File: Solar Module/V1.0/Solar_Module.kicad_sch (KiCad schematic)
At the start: 8 parts, among them U1 MT3608

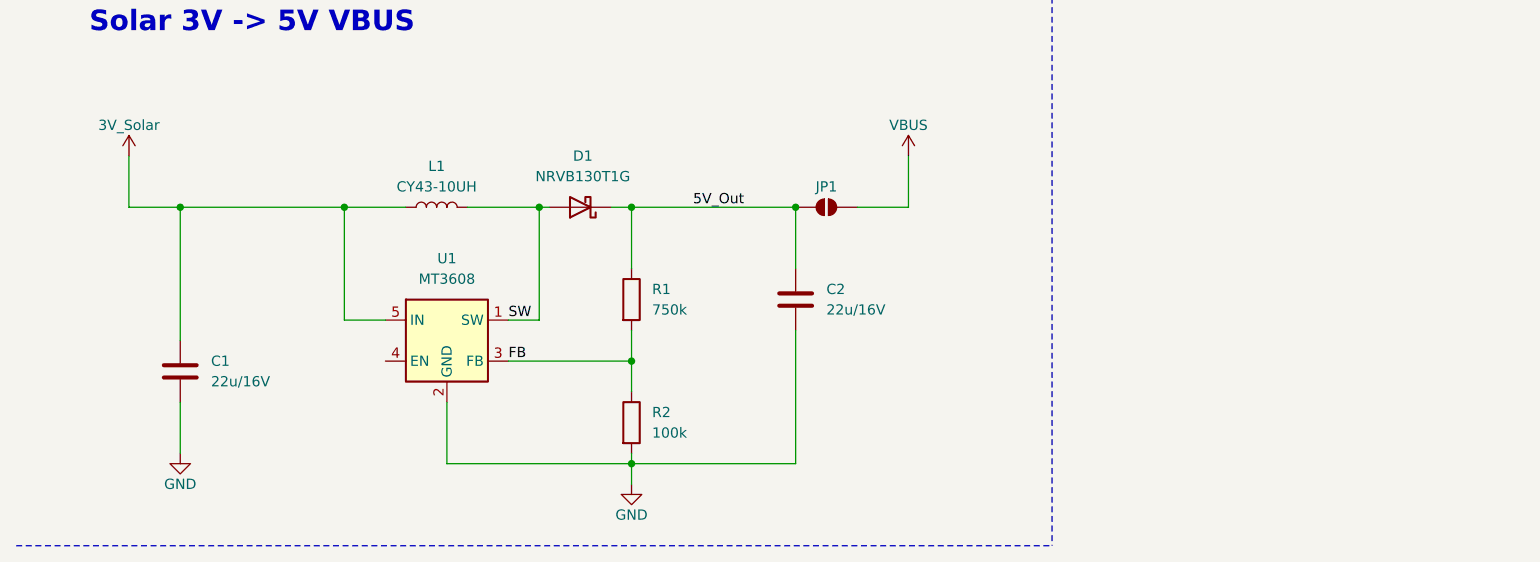
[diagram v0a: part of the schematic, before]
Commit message: Added TP4057 to Schematic.
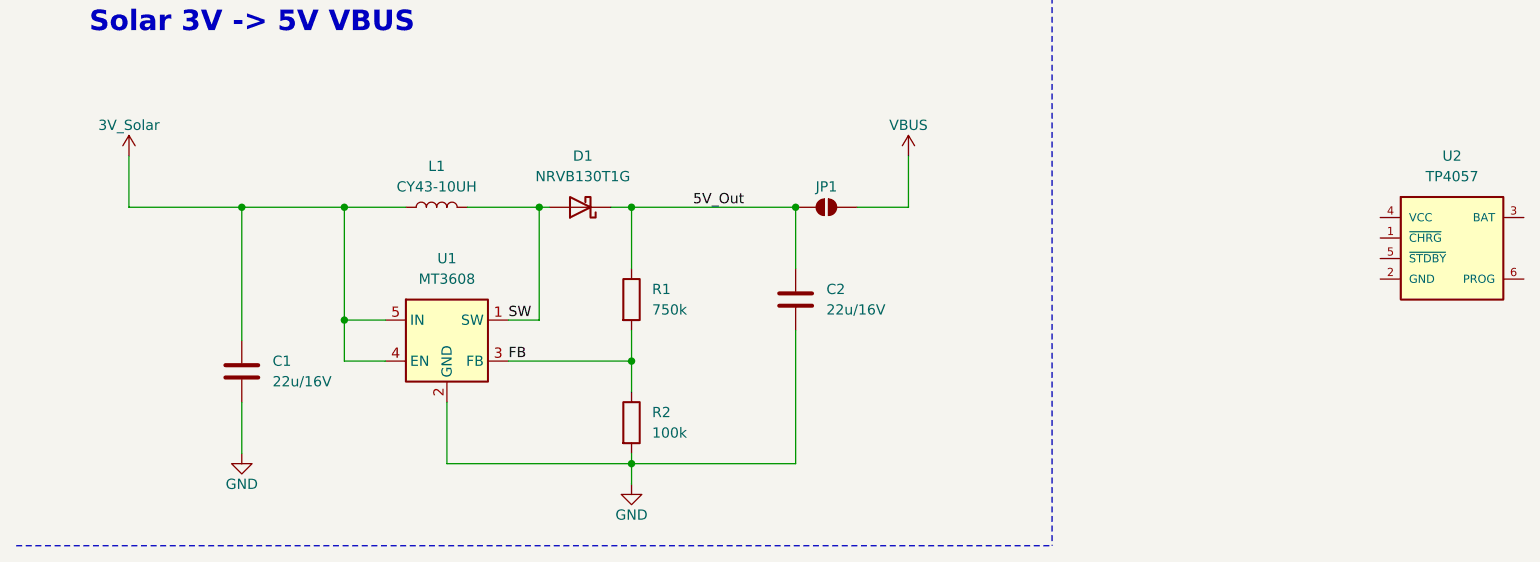
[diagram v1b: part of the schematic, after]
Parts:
- added U2: TP4057, Package_TO_SOT_SMD:SOT-23-6, symbol Private_Power_Modules:TP4057
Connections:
- net 3V_Solar: now also U1.4 (EN)
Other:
- moved on the sheet: C1
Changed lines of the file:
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@@
+	)
+	(junction
+		(at 39.37 46.99)
+		(diameter 0)
+		(color 0 0 0 0)
 	)
 	(junction
@@
 	)
 	(junction
-		(at 31.75 46.99)
-		(diameter 0)
-		(color 0 0 0 0)
-	)
-	(junction
 		(at 52.07 46.99)
 		(diameter 0)
@@
 		(color 0 0 0 0)
 	)
+	(junction
+		(at 52.07 60.96)
+		(diameter 0)
+		(color 0 0 0 0)
+	)
 	(polyline
 		(pts
@@
 	(wire
 		(pts
-			(xy 31.75 46.99) (xy 52.07 46.99)
-		)
-		(stroke
-			(width 0)
-			(type default)
-		)
-	)
-	(wire
-		(pts
 			(xy 52.07 60.96) (xy 57.15 60.96)
 		)
@@
 	(wire
 		(pts
-			(xy 31.75 46.99) (xy 31.75 63.5)
+			(xy 39.37 46.99) (xy 39.37 63.5)
 		)
 		(stroke
@@
 	(wire
 		(pts
-			(xy 31.75 46.99) (xy 25.4 46.99)
+			(xy 25.4 46.99) (xy 39.37 46.99)
 		)
 		(stroke
@@
 	(wire
 		(pts
-			(xy 31.75 71.12) (xy 31.75 77.47)
+			(xy 39.37 71.12) (xy 39.37 77.47)
 		)
 		(stroke
@@
 		(pts
 			(xy 52.07 46.99) (xy 59.69 46.99)
+		)
+		(stroke
+			(width 0)
+			(type default)
+		)
+	)
+	(wire
+		(pts
+			(xy 52.07 66.04) (xy 52.07 60.96)
+		)
+		(stroke
+			(width 0)
+			(type default)
+		)
+	)
+	(wire
+		(pts
+			(xy 57.15 66.04) (xy 52.07 66.04)
+		)
+		(stroke
+			(width 0)
+			(type default)
+		)
+	)
+	(wire
+		(pts
+			(xy 39.37 46.99) (xy 52.07 46.99)
 		)
 		(stroke
@@
 	(symbol
 		(lib_id "power:GND")
-		(at 31.75 77.47 0)
+		(at 39.37 77.47 0)
 		(unit 1)
 		(exclude_from_sim no)
@@
 		(dnp no)
 		(property "Reference" "#PWR02"
-			(at 31.75 83.82 0)
+			(at 39.37 83.82 0)
 			(effects
 				(font
@@
 		)
 		(property "Value" "GND"
-			(at 31.75 81.28 0)
+			(at 39.37 81.28 0)
 			(effects
 				(font
@@
 		)
 		(property "Footprint" ""
-			(at 31.75 77.47 0)
+			(at 39.37 77.47 0)
 			(effects
 				(font
@@
 		)
 		(property "Datasheet" ""
-			(at 31.75 77.47 0)
+			(at 39.37 77.47 0)
 			(effects
 				(font
@@
 		)
 		(property "Description" "Power symbol creates a global label with name \"GND\" , ground"
-			(at 31.75 77.47 0)
+			(at 39.37 77.47 0)
 			(effects
 				(font
@@
 	(symbol
 		(lib_id "Device:C")
-		(at 31.75 67.31 0)
+		(at 39.37 67.31 0)
 		(unit 1)
 		(exclude_from_sim no)
@@
 		(fields_autoplaced yes)
 		(property "Reference" "C1"
-			(at 35.56 66.0399 0)
+			(at 43.18 66.0399 0)
 			(effects
 				(font
@@
 		)
 		(property "Value" "22u/16V"
-			(at 35.56 68.5799 0)
+			(at 43.18 68.5799 0)
 			(effects
 				(font
@@
 		)
 		(property "Footprint" ""
-			(at 32.7152 71.12 0)
+			(at 40.3352 71.12 0)
 			(effects
 				(font
@@
 		)
 		(property "Datasheet" "~"
-			(at 31.75 67.31 0)
+			(at 39.37 67.31 0)
 			(effects
 				(font
@@
 		)
 		(property "Description" "Unpolarized capacitor"
-			(at 31.75 67.31 0)
+			(at 39.37 67.31 0)
 			(effects
 				(font
@@
 					(unit 1)
 				)
+			)
+		)
+	)
+	(symbol
+		(lib_id "Private_Power_Modules:TP4057")
+		(at 187.96 50.8 0)
+		(unit 1)
+		(exclude_from_sim no)
+		(in_bom yes)
+		(on_board yes)
+		(dnp no)
+		(fields_autoplaced yes)
+		(property "Reference" "U2"
+			(at 189.23 40.64 0)
+			(effects
+				(font
+					(size 1.27 1.27)
+				)
+			)
+		)
+		(property "Value" "TP4057"
+			(at 189.23 43.18 0)
+			(effects
+				(font
+					(size 1.27 1.27)
+				)
+			)
+		)
+		(property "Footprint" "Package_TO_SOT_SMD:SOT-23-6"
+			(at 187.198 73.914 0)
+			(effects
+				(font
+					(size 1.27 1.27)
+				)
+				(justify bottom)
+				(hide yes)
+			)
+		)
+		(property "Datasheet" "http://toppwr.com/uploadfile/file/20230304/640302a47b738.pdf"
+			(at 187.198 74.168 0)
+			(effects
+				(font
+					(size 1.27 1.27)
+				)
+				(hide yes)
+			)
+		)
+		(property "Description" ""
+			(at 187.198 74.168 0)
+			(effects
+				(font
+					(size 1.27 1.27)
+				)
+				(hide yes)
+			)
+		)
+		(property "MF" "toppower"
+			(at 187.198 74.168 0)
+			(effects
+				(font
+					(size 1.27 1.27)
+				)
+				(justify bottom)
+				(hide yes)
+			)
+		)
+		(property "Description_1" "\nSOT23-6 BATTERY MANAGEMENT ICS R\n"
+			(at 187.96 73.914 0)
+			(effects
+				(font
+					(size 1.27 1.27)
+				)
+				(justify bottom)
+				(hide yes)
+			)
+		)
+		(property "Package" "None"
+			(at 187.96 73.406 0)
+			(effects
+				(font
+					(size 1.27 1.27)
+				)
+				(justify bottom)
+				(hide yes)
+			)
+		)
+		(property "Price" "None"
+			(at 187.452 73.152 0)
+			(effects
+				(font
+					(size 1.27 1.27)
+				)
+				(justify bottom)
+				(hide yes)
+			)
+		)
+		(property "SnapEDA_Link" "https://www.snapeda.com/parts/TP4057/Top+Power/view-part/?ref=snap"
+			(at 189.23 73.914 0)
+			(effects
+				(font
+					(size 1.27 1.27)
+				)
+				(justify bottom)
+				(hide yes)
+			)
+		)
+		(property "MP" "TP4057"
+			(at 187.198 74.168 0)
+			(effects
+				(font
+					(size 1.27 1.27)
+				)
+				(justify bottom)
+				(hide yes)
+			)
+		)
+		(property "Availability" "Not in stock"
+			(at 187.198 74.168 0)
+			(effects
+				(font
+					(size 1.27 1.27)
+				)
+				(justify bottom)
+				(hide yes)
+			)
+		)
+		(property "Check_prices" "https://www.snapeda.com/parts/TP4057/Top+Power/view-part/?ref=eda"
+			(at 189.23 73.914 0)
+			(effects
+				(font
+					(size 1.27 1.27)
+				)
+				(justify bottom)
+				(hide yes)
+			)
+		)
+		(pin "4"
+		)
+		(pin "6"
+		)
+		(pin "1"
+		)
+		(pin "2"
+		)
+		(pin "3"
+		)
+		(pin "5"
+		)
+		(instances
+			(project "Solar_Module"
+				(path "/6feb19b9-d88e-42ef-ad0c-10449181595e"
+					(reference "U2")
+					(unit 1)
+				)

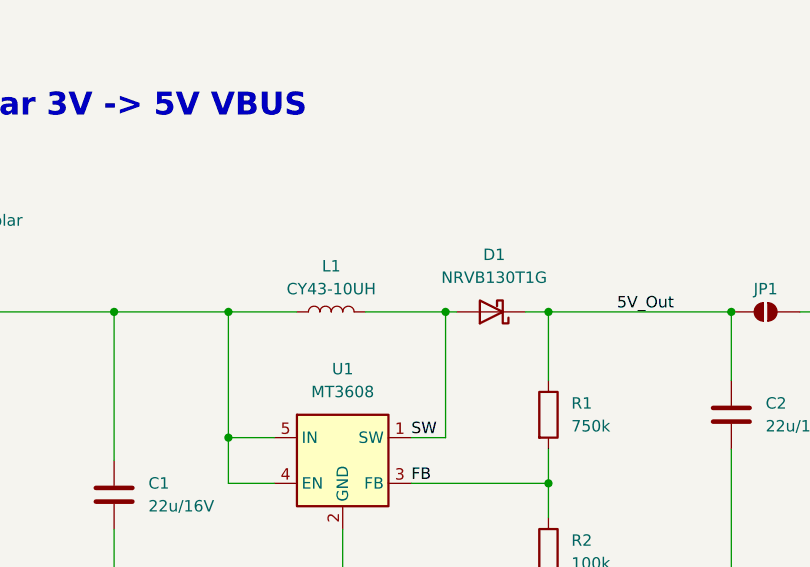
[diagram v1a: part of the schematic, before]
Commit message: Updated Buck Converter Passives.
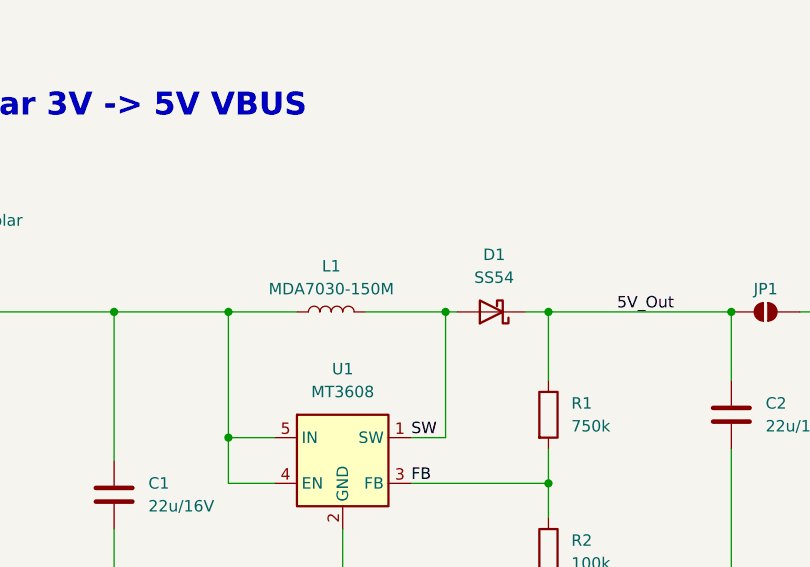
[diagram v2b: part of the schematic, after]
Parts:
- D1: value NRVB130T1G -> SS54; footprint Diode_SMD:D_SOD-123 -> Diode_SMD:D_SMA
- L1: value CY43-10UH -> MDA7030-150M; footprint Inductor_SMD:L_Ferrocore_DLG-0403 -> Inductor_SMD:L_Sunlord_MWSA0603S
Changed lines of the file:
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@@
 			)
 		)
-		(property "Value" "NRVB130T1G"
+		(property "Value" "SS54"
 			(at 81.5975 43.18 0)
 			(effects
@@
 			)
 		)
-		(property "Footprint" "Diode_SMD:D_SOD-123"
+		(property "Footprint" "Diode_SMD:D_SMA"
 			(at 81.28 46.99 0)
 			(effects
@@
 			)
 		)
-		(property "Value" "CY43-10UH"
+		(property "Value" "MDA7030-150M"
 			(at 63.5 44.45 90)
 			(effects
@@
 			)
 		)
-		(property "Footprint" "Inductor_SMD:L_Ferrocore_DLG-0403"
+		(property "Footprint" "Inductor_SMD:L_Sunlord_MWSA0603S"
 			(at 63.5 46.99 0)
 			(effects

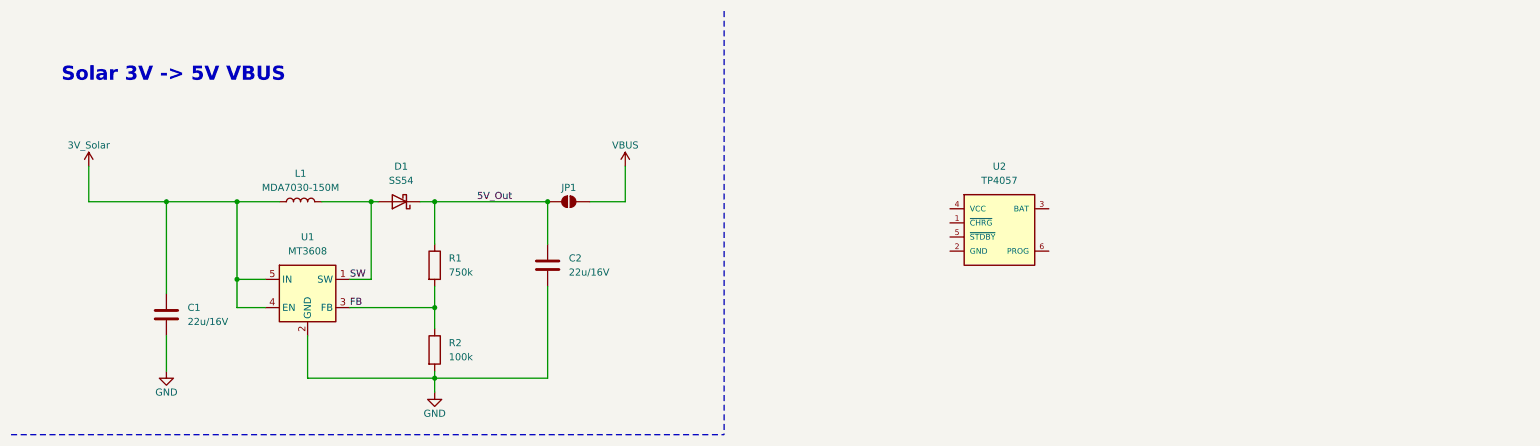
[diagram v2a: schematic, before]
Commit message: Schematic of TP4057 should be finished.
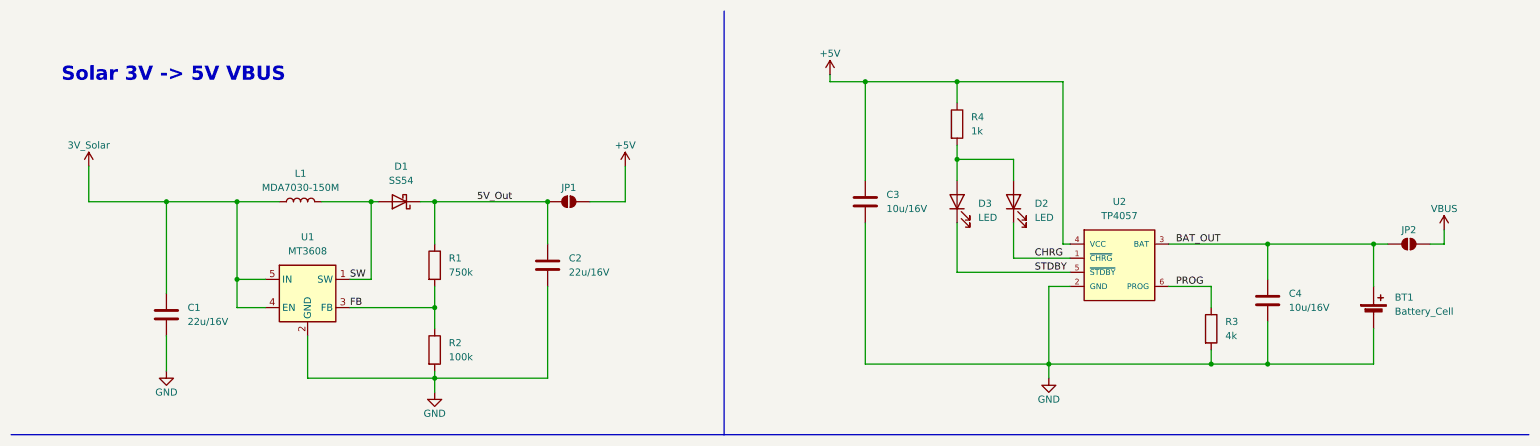
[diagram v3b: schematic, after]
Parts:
- added BT1: Battery_Cell, symbol Device:Battery_Cell
- added C3, C4: 10u/16V, symbol Device:C
- added D2, D3: LED, symbol Device:LED
- added JP2: SolderJumper_2_Open, symbol Jumper:SolderJumper_2_Open
- added R3: 4k, symbol Device:R
- added R4: 1k, symbol Device:R
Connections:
- net GND: now also U2.2 (GND), BT1.2 (-), C3.2, C4.2, R3.2
- net VBUS: now also JP2.2 (B); no longer JP1.2 (B)
- net CHRG: now reaches U2.1 (~{CHRG})
- net CHRG: now also D2.1 (K)
- net BAT_OUT: now reaches U2.3 (BAT)
- net BAT_OUT: now also BT1.1 (+), C4.1, JP2.1 (A)
- net +5V: now reaches U2.4 (VCC)
- net +5V: now also JP1.2 (B), C3.1, R4.1
- net STDBY: now reaches U2.5 (~{STDBY})
- net STDBY: now also D3.1 (K)
- net PROG: now reaches U2.6 (PROG)
- net PROG: now also R3.1
- new net: D2.2 (A), D3.2 (A), R4.2
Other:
- moved on the sheet: U2

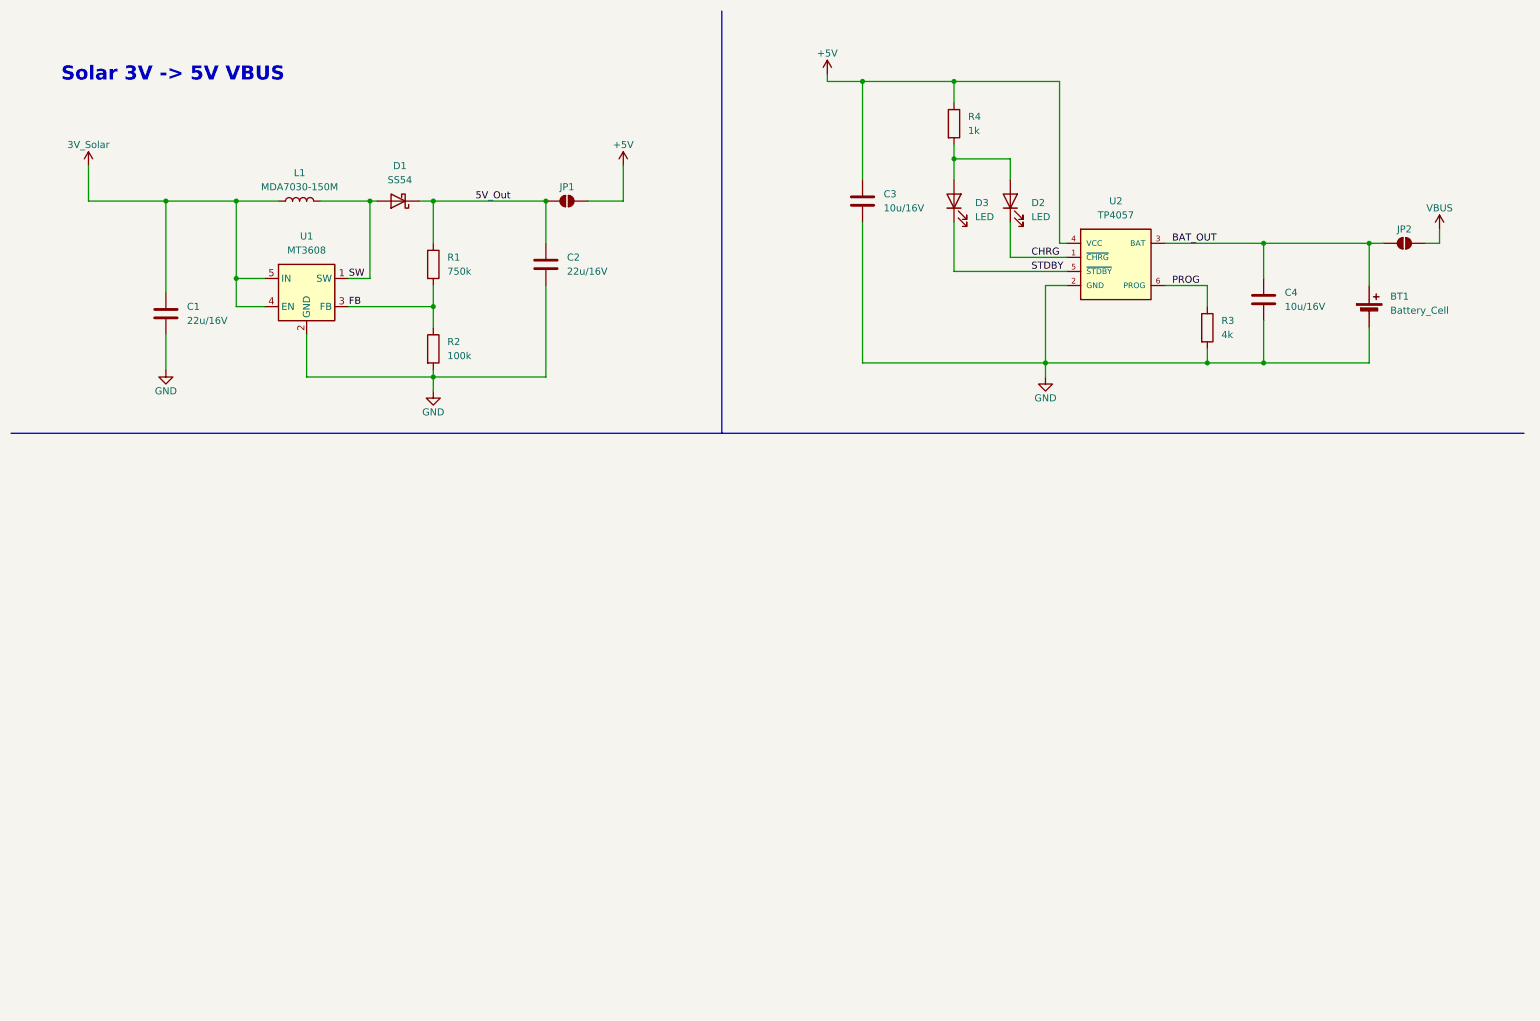
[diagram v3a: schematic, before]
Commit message: Added Connector for Akku.
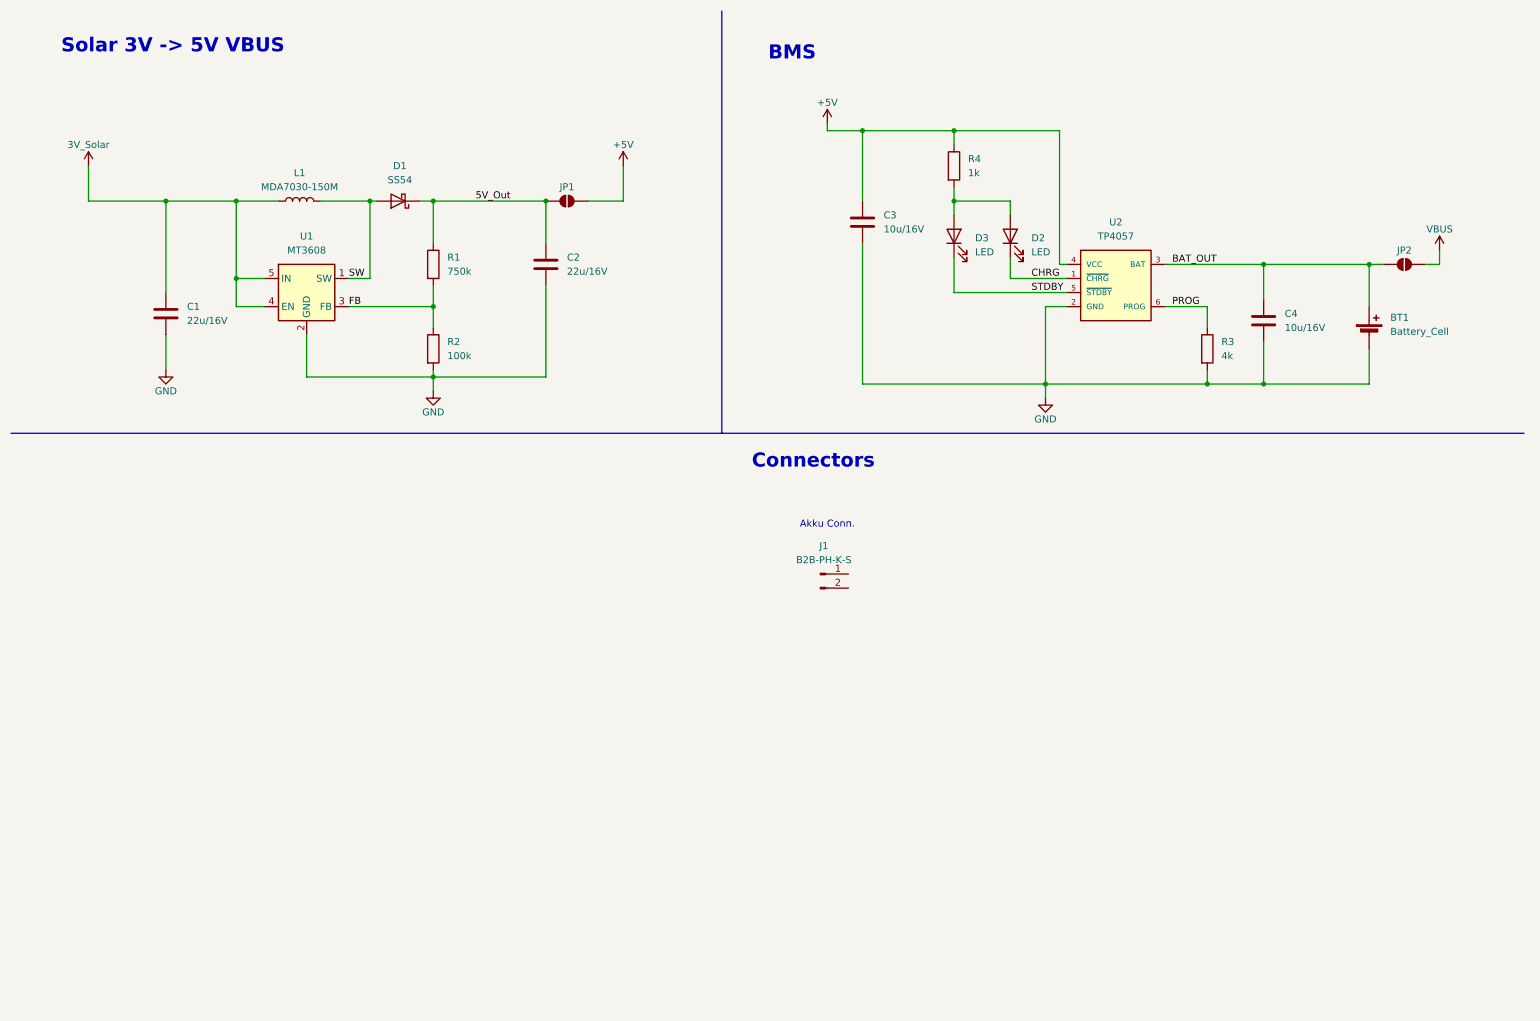
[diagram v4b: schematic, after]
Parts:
- added J1: B2B-PH-K-S, Connector_JST:JST_EH_B2B-EH-A_1x02_P2.50mm_Vertical, symbol Connector:Conn_01x02_Pin
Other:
- note added: "Akku Conn."
- note added: "BMS"
- note added: "Connectors"
- moved on the sheet: BT1, C3, C4, D2, D3, JP2, R3, R4, U2
